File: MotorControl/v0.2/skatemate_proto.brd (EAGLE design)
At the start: 167.4 x 87.6 mm, 97 parts, among them IC1 REG1117, U1 DRV8301DCAR

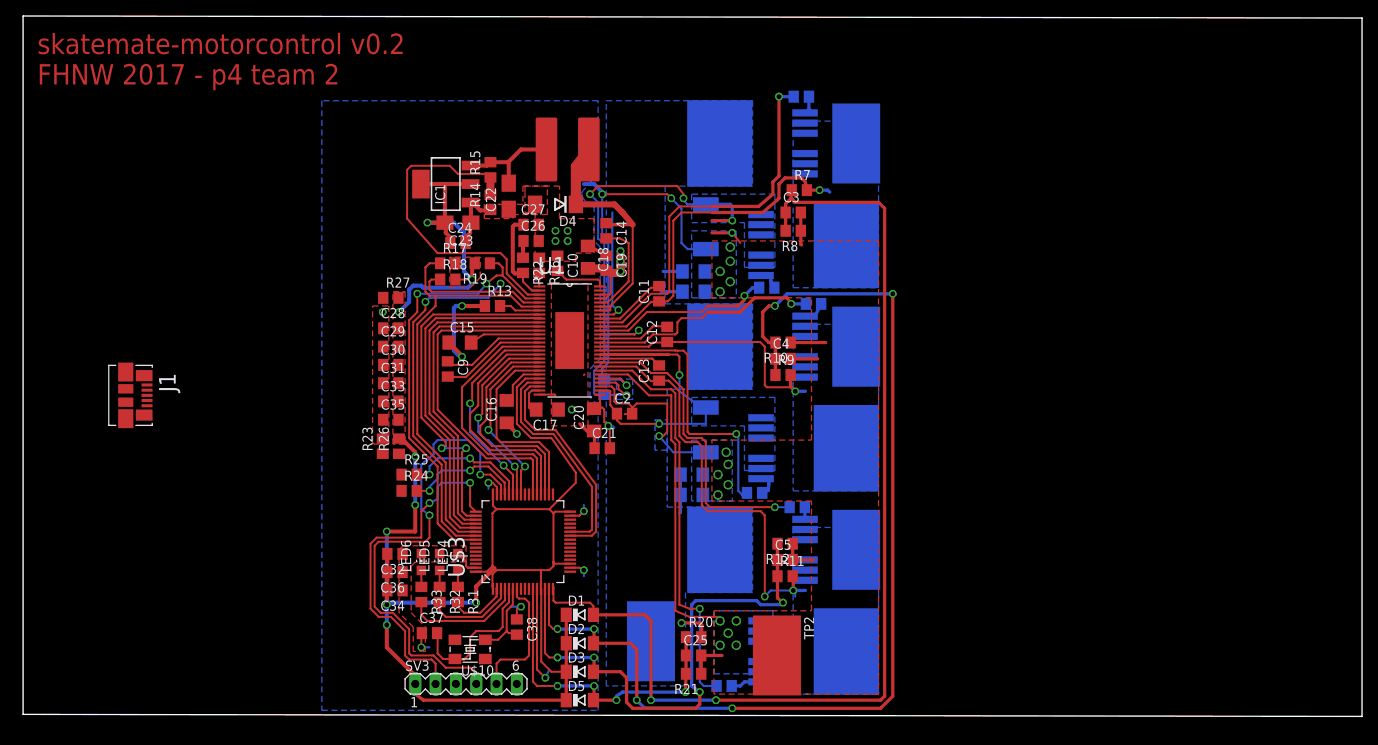
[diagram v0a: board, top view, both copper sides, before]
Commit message: renumber parts and bom
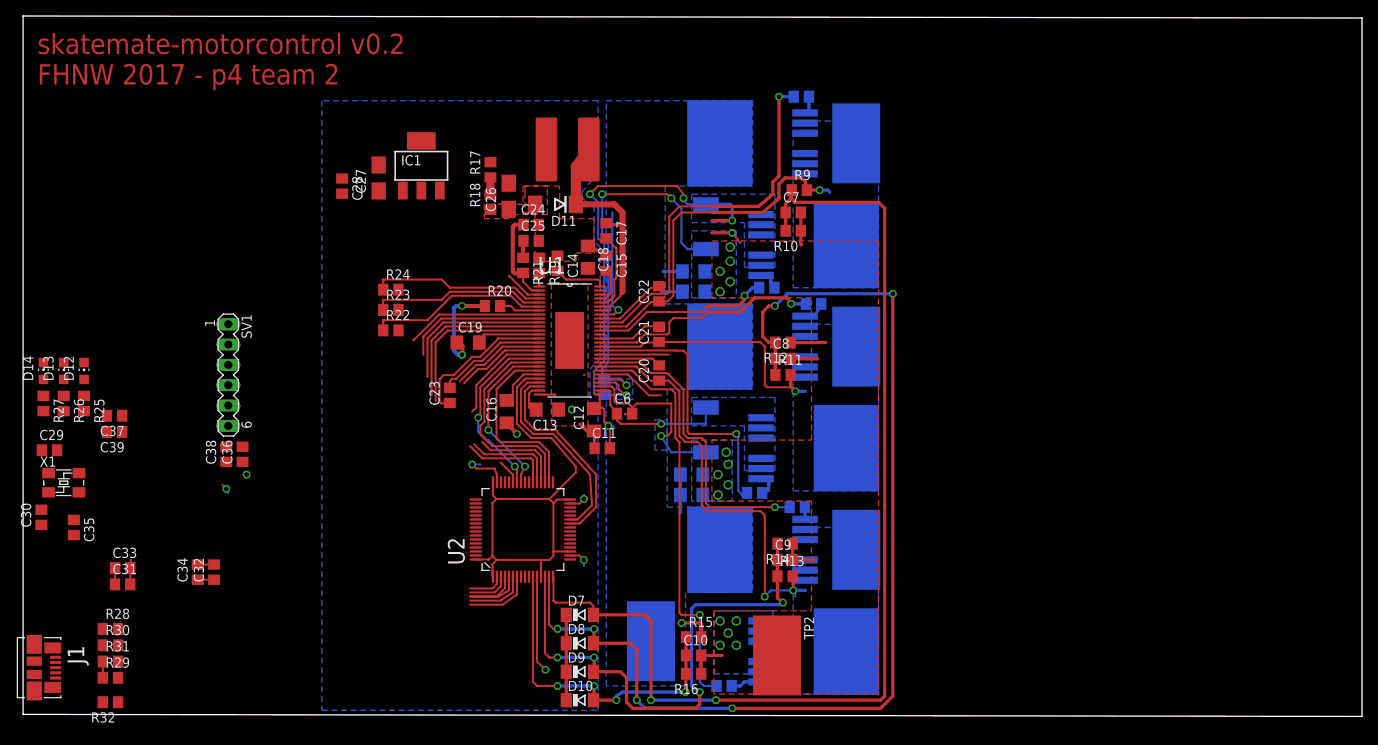
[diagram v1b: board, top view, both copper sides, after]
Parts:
- removed LED4, LED5, LED6: (no value), skatemate:CHIP-LED0805
- removed R33: 3k3, skatemate:R0805
- removed SV3: (no value), skatemate:MA06-1
- removed U$1, U$2: R_EU, skatemate:R2512
- removed U$10: ABM3B, skatemate:IQG5032B
- removed U$3: STM32F303XD/XELQFP64, skatemate:LQFP64
- removed U$4, U$5, U$6, U$7, U$8: IRFS7534, skatemate:D2PAK-7
- added D10, D7, D8, D9: BAS85, skatemate:SOD80C
- added D11: SSA210, skatemate:DO-214AA
- added D12, D13, D14: (no value), skatemate:CHIP-LED0805
- added R28: 0*, skatemate:R0805
- added R29: 1k5, skatemate:R0805
- added R30: 22, skatemate:R0805
- added SV1: (no value), skatemate:MA06-1
- added U2: STM32F303XD/XELQFP64, skatemate:LQFP64
- added X1: ABM3B, skatemate:IQG5032B
- C1: value (none) -> 2n2
- C10: value 10nF -> 47p
- C12: value 0.1u -> 4u7; device skatemate:C0805 -> skatemate:C1206
- C13: value 0.1u -> 1u; device skatemate:C0805 -> skatemate:C1206
- C14: value 0.1u -> 10n
- C15: value 2.2u -> 0.1u; device skatemate:C1206 -> skatemate:C0805
- C17: value 1u -> 0.1u; device skatemate:C1206 -> skatemate:C0805
- C18: value 4.7u -> 4u7
- C19: value 0.1u -> 2u2; device skatemate:C0805 -> skatemate:C1206
- C2: value (none) -> 2u2; device skatemate:C0805 -> skatemate:C1206
- C20: value 4.7u -> 0.1u; device skatemate:C1206 -> skatemate:C0805
- C22: value 100u -> 0.1u; device skatemate:B/3528-21W -> skatemate:C0805
- C23: value 100u -> (none); device skatemate:B/3528-21W -> skatemate:C0805
- C24: value 0.1u -> 150p
- C25: value 47p -> 6n8
- C26: value 6n8 -> 100u; device skatemate:C0805 -> skatemate:B/3528-21W
- C27: value 150p -> 100u; device skatemate:C0805 -> skatemate:B/3528-21W
- C28: value 2u2 -> 0.1u
- C29: value 2u2 -> 22p
- C3, C4, C5: value 47p -> 2u2; device skatemate:C0805 -> skatemate:C1206
- C30: value 100n -> 22p
- C31, C32, C36: value 100n -> 2u2
- C33, C34: value 2u2 -> 100n
- C37: value 22p -> 2u2
- C38: value 22p -> 100n
- C39: value 2u2 -> 100n; device skatemate:C1206 -> skatemate:C0805
- C6: value 2u2 -> 2n2; device skatemate:C1206 -> skatemate:C0805
- C7, C8: value 2u2 -> 47p; device skatemate:C1206 -> skatemate:C0805
- C9: value (none) -> 47p
- D1, D2, D3, D5: value BAS85 -> IRFS7534; device skatemate:SOD80C -> skatemate:D2PAK-7
- D4: value SSA210 -> IRFS7534; device skatemate:DO-214AA -> skatemate:D2PAK-7
- L1: value (none) -> 22u
- R1, R2, R4, R5: value (none) -> 10
- R13: value 10k -> 39k
- R14: value 3k3 -> 2k2
- R15: value 18k -> 39k
- R16: value 220k -> 2k2
- R18: value 18k -> 3k3
- R19: value 18k -> 220k
- R20: value 39k -> 10k
- R21: value 2k2 -> 16k
- R22: value 16k -> 18k
- R23: value 100k -> 18k
- R24: value 22 -> 18k
- R25: value 22 -> 3k3
- R26: value 1k5 -> 3k3
- R27: value 0 * -> 3k3
- R3, R6: value (none) -> 1m; device skatemate:R0805 -> skatemate:R2512
- R31: value 3k3 -> 22
- R32: value 3k3 -> 100k
- R7: value 39k -> 10
- R8: value 2k2 -> 10
- moved C39 75.1 mm to (11.4, 35.3), flipped to the top
- moved R15 63.7 mm to (83.8, 9.65), turned to 0 degrees
- moved D1 62.8 mm to (91.2, 71.4), flipped to the bottom, turned to 270 degrees
- moved D2 57.7 mm to (98.8, 58.7), flipped to the bottom, turned to 90 degrees
- moved R8 57.5 mm to (87.6, 3.56), flipped to the bottom
- moved R14 56.4 mm to (95.2, 21.3), turned to 180 degrees
- moved C25 55.7 mm to (63.5, 59.2)
- moved R21 55.3 mm to (62.5, 56.1), turned to 270 degrees
- moved R16 54.6 mm to (83.8, 5.08), turned to 180 degrees
- moved C10 51.9 mm to (83.8, 7.37), turned to 0 degrees
- moved R13 49.8 mm to (95.2, 17.3)
- moved C9 48.5 mm to (95.2, 19.3), turned to 0 degrees
- moved R20 48.4 mm to (58.7, 51.1)
- moved C37 47.8 mm to (11.4, 37.3), turned to 180 degrees
- moved C30 47.7 mm to (2.29, 24.6), turned to 90 degrees
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- renumbered U$9 to D6
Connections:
- net +5V: now also C26.+, R17.2; no longer C22.+, R15.2
- net ASENSE: now also C7.1, D7.A, R10.2, R9.1, U2.16; no longer C3.1, D1.A, R7.1, R8.2, U$3.16
- net BSENSE: now also C8.1, D8.A, R11.1, R12.2, U2.15; no longer C4.1, D2.A, R10.2, R9.1, U$3.15
- net BST_BK: now also C17.1, D11.C; no longer C14.1, D4.C
- net CSENSE: now also C9.1, D9.A, R13.1, R14.2, U2.14; no longer C5.1, D3.A, R11.1, R12.2, U$3.14
- net DRV_DCCAL: now also U2.38; no longer U$3.38
- net DRV_EN_GATE: now also U2.37; no longer U$3.37
- net DRV_NCS: now also U2.50; no longer U$3.50
- net DRV_NFAULT: now also R22.1, U2.54; no longer R17.1, U$3.54
- net DRV_NOCTW: now also R23.1, U2.55; no longer R18.1, U$3.55
- net DRV_PWRGD: now also R24.1, U2.56; no longer R19.1, U$3.56
- net DRV_SCK: now also U2.51; no longer U$3.51
- net DRV_SDI: now also U2.53; no longer U$3.53
- net DRV_SDO: now also U2.52; no longer U$3.52
- net DRV_SOA: now also U2.27; no longer U$3.27
- net DRV_SOB: now also U2.26; no longer U$3.26
- net GH_B: now also R4.1; no longer R3.1
- net GH_C: now also R7.1; no longer R5.1
- net GL_B: now also R5.1; no longer R4.1
- net GL_C: now also R8.1; no longer R6.1
- net GND: now also C10.2, C11.1, C12.1, C13.1, C14.1, C26.-, C27.-, C28.2, C39.1, C9.2, D11.A, D12.C, D13.C, D14.C, R18.1, R19.1, R20.1, R3.2, R32.2, R6.2, SV1.3, U2.12, U2.18, U2.31, U2.47, U2.63; no longer C10.1, C17.1, C20.1, C21.1, C22.-, C23.-, C26.2, C27.2, C28.1, C39.2, D4.A, LED4.C, LED5.C, LED6.C, R13.1, R21.1, R23.2, R8.1, SV3.3, U$1.2, U$2.2, U$3.12, U$3.18, U$3.31, U$3.47, U$3.63
- net INH_A: now also U2.43; no longer U$3.43
- net INH_B: now also U2.42; no longer U$3.42
- net INH_C: now also U2.41; no longer U$3.41
- net INL_A: now also U2.36; no longer U$3.36
- net INL_B: now also U2.35; no longer U$3.35
- net INL_C: now also U2.34; no longer U$3.34
- net N$1: now also C23.2; no longer C9.2
- net N$10: now also D3.G, R4.2; no longer R3.2, U$6.G
- net N$11: now also D5.G, R7.2; no longer R5.2, U$8.G
- net N$12: now also R8.2; no longer R6.2
- net N$13: now also C22.2; no longer C11.2
- net N$14: now also C21.2; no longer C12.2
- net N$15: now also C20.2; no longer C13.2
- net N$16: now also C17.2; no longer C14.2
- net N$17: now also C19.2; no longer C15.2
- net N$19: now also C13.2; no longer C17.2
- net N$2: now also C23.1; no longer C9.1
- net N$20: now also C24.1, R21.2; no longer C27.1, R22.2
- net N$21: now also C25.1, R21.1; no longer C26.1, R22.1
- net N$22: now also R32.1; no longer R23.1
- net N$23: now also R29.1, R31.1; no longer R24.1, R26.1
- net N$24: now also R30.1; no longer R25.1
- net N$25: now also R28.1; no longer R27.1
- net N$28: now also R27.2, U2.4; no longer R33.2, U$3.4
- net N$29: now also R26.2, U2.3; no longer R32.2, U$3.3
- net N$3: now also R20.2; no longer R13.2
- net N$30: now also R25.2, U2.2; no longer R31.2, U$3.2
- net N$31: now also D12.A, R25.1; no longer LED4.A, R31.1
- net N$32: now also D13.A, R26.1; no longer LED5.A, R32.1
- net N$33: now also D14.A, R27.1; no longer LED6.A, R33.1
- net N$35: now also C30.2, U2.6, X1.1; no longer C38.2, U$10.1, U$3.6
- net N$36: now also C29.2, U2.5, X1.3; no longer C37.2, U$10.3, U$3.5
- net N$4: now also R17.1, R18.2; no longer R14.2, R15.1
- net N$5: now also C14.2; no longer C10.2
- net N$6: now also R19.2; no longer R16.2
- net N$7: now also D1.G; no longer U$4.G
- net N$8: now also D2.G; no longer U$5.G
- net N$9: now also D4.G, R5.2; no longer R4.2, U$7.G
- net NRST: now also SV1.5, U2.7; no longer SV3.5, U$3.7
- net PH_A: now also C22.1, D1.S1, D1.S2, D1.S3, D1.S4, D1.S5, D2.D, R9.2; no longer C11.1, R7.2, U$4.S1, U$4.S2, U$4.S3, U$4.S4, U$4.S5, U$5.D
- net PH_B: now also C21.1, D3.S1, D3.S2, D3.S3, D3.S4, D3.S5, D4.D, R11.2; no longer C12.1, R9.2, U$6.S1, U$6.S2, U$6.S3, U$6.S4, U$6.S5, U$7.D
- net PH_C: now also C20.1, D5.S1, D5.S2, D5.S3, D5.S4, D5.S5, R13.2; no longer C13.1, R11.2, U$8.S1, U$8.S2, U$8.S3, U$8.S4, U$8.S5
- net SN_A: now also D2.S1, D2.S2, D2.S3, D2.S4, D2.S5, R3.1; no longer U$1.1, U$5.S1, U$5.S2, U$5.S3, U$5.S4, U$5.S5
- net SN_B: now also C6.1, D4.S1, D4.S2, D4.S3, D4.S4, D4.S5, R6.1; no longer C2.1, U$2.1, U$7.S1, U$7.S2, U$7.S3, U$7.S4, U$7.S5
- net SSENSE: now also C10.1, D10.A, R15.1, R16.2, U2.11; no longer C25.1, D5.A, R20.1, R21.2, U$3.11
- net SUPPLY: now also C11.2, C12.2, C15.2, C2.1, C3.1, C4.1, C5.1, D1.D, D3.D, D5.D, R15.2; no longer C19.2, C20.2, C21.2, C39.1, C6.1, C7.1, C8.1, R20.2, U$4.D, U$6.D, U$8.D
- net SWCLK: now also SV1.2, U2.49; no longer SV3.2, U$3.49
- net SWDIO: now also SV1.4, U2.46; no longer SV3.4, U$3.46
- net USART3_RX: now also U2.30; no longer U$3.30
- net USART3_TX: now also U2.29; no longer U$3.29
- net USB_D+: now also R31.2, U2.45; no longer R24.2, U$3.45
- net USB_D-: now also R30.2, U2.44; no longer R25.2, U$3.44
- net VCC: now also C27.+, C28.1, C37.2, C38.2, C39.2, D10.C, D7.C, D8.C, D9.C, R22.2, R23.2, R24.2, R28.2, R29.2, SV1.1, U2.1, U2.13, U2.19, U2.32, U2.48, U2.64; no longer C23.+, C24.1, C28.2, C29.2, C30.2, D1.C, D2.C, D3.C, D5.C, R17.2, R18.2, R19.2, R26.2, R27.2, SV3.1, U$3.1, U$3.13, U$3.19, U$3.32, U$3.48, U$3.64
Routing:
- net VCC: track 232.2 -> 96.6 mm, vias 10 -> 1
- net SWDIO: track 60.8 -> 0.00 mm, vias 2 -> 0
- net GND: track 210.9 -> 162.5 mm, vias 35 -> 29
- net SWCLK: track 46.2 -> 0.00 mm, vias 2 -> 0
- net DRV_NOCTW: track 62.8 -> 21.9 mm, vias 2 -> 0
- net DRV_PWRGD: track 56.4 -> 21.9 mm, vias 2 -> 0
- net N$4: track 41.3 -> 6.99 mm
- net DRV_NFAULT: track 54.9 -> 22.7 mm
- net DRV_NCS: track 45.3 -> 17.1 mm, vias 2 -> 0
- net DRV_SDI: track 43.7 -> 17.7 mm
- net DRV_SDO: track 41.7 -> 19.7 mm
- net DRV_SCK: track 40.0 -> 21.1 mm
- net SN_B: track 44.1 -> 27.2 mm, vias 2 -> 1
- net USB_D+: track 15.2 -> 0.00 mm, vias 2 -> 0
- net USB_D-: track 15.8 -> 1.25 mm, vias 2 -> 1
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- removed copper zone on layer 1, net VCC
